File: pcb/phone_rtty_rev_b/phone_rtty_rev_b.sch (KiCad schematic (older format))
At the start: 33 parts, among them J1 Phone, J2 Transceiver, P1 TRX Data, Q1 2N2222, Q2 2N2222, SW1 1200/9600

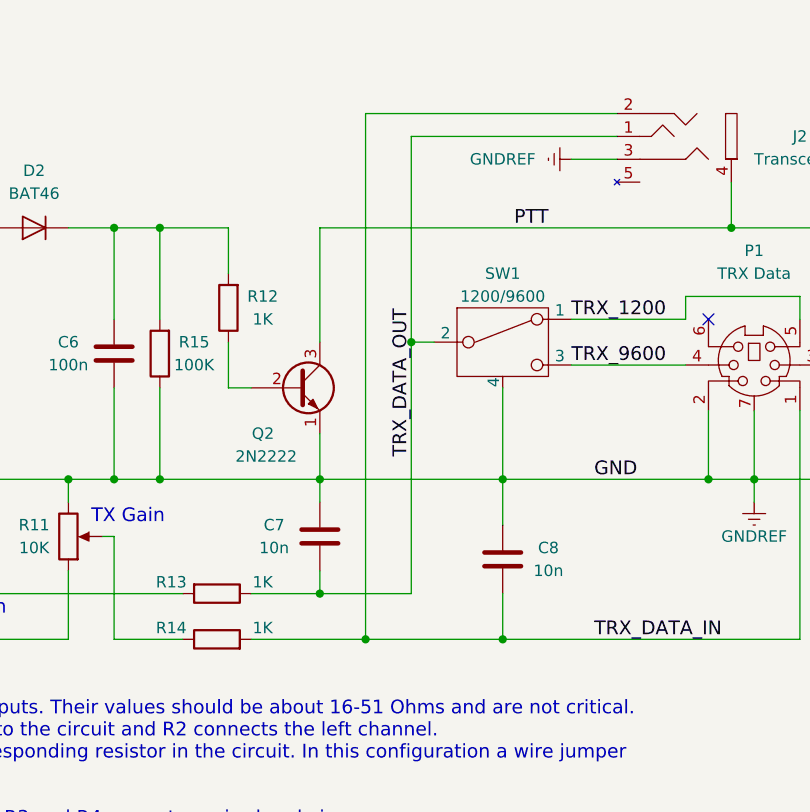
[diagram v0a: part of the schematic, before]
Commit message: Main board and panels corrections.
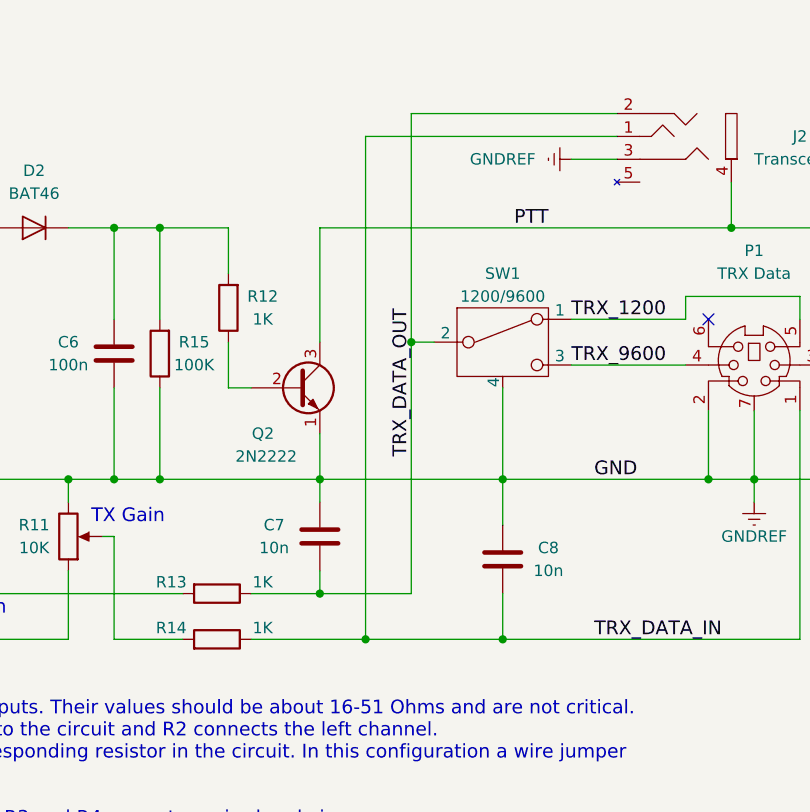
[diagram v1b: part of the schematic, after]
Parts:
- J1, J2: footprint custom_kicad_footprints:PJ320E_Headphones_Plug_Short -> Phone_RTTY_Footprints:PJ320E_3.5mm_Jack
- P1: footprint custom_kicad_footprints:Connector_Mini-DIN_Female_6Pin_2rows -> Phone_RTTY_Footprints:Connector_Mini-DIN_Female_6Pin_2rows
- R10, R11: footprint custom_kicad_footprints:Potentiometer_Trimmer_Vertical_Multi_Compatible -> Phone_RTTY_Footprints:Potentiometer_Trimmer_Vertical_Multi_Compatible
- SW1: footprint custom_kicad_footprints:Cliff_UT1x_SPDT_ON-ON_Switch_Short -> Phone_RTTY_Footprints:Cliff_UT1x_SPDT_ON-ON_Switch_Short
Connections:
- net GNDREF: now also C7.2, C8.2; no longer C7.1, C8.1
- net TRX_DATA_IN: now also C8.1, J2.1 (R), R14.1; no longer C8.2, J2.2 (L), R14.2
- net TRX_DATA_OUT: now also C7.1, J2.2 (L); no longer C7.2, J2.1 (R)
- net at R11.2: now also R14.2; no longer R14.1
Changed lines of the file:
@@
 U 1 1 5829EA63
 P 7900 3750
-F 0 "C8" H 8100 3800 50  0000 C CNN
-F 1 "10n" H 8100 3700 50  0000 C CNN
+F 0 "C8" H 8100 3700 50  0000 C CNN
+F 1 "10n" H 8100 3800 50  0000 C CNN
 F 2 "Capacitors_THT:C_Disc_D4.3mm_W1.9mm_P5.00mm" H 7938 3600 50  0001 C CNN
 F 3 "" H 7900 3750 50  0000 C CNN
 	1    7900 3750
-	1    0    0    -1
+	1    0    0    1
 $EndComp
 $Comp
@@
 U 1 1 5829EAA2
 P 7100 3650
-F 0 "C7" H 6900 3700 50  0000 C CNN
-F 1 "10n" H 6900 3600 50  0000 C CNN
+F 0 "C7" H 6900 3600 50  0000 C CNN
+F 1 "10n" H 6900 3700 50  0000 C CNN
 F 2 "Capacitors_THT:C_Disc_D4.3mm_W1.9mm_P5.00mm" H 7138 3500 50  0001 C CNN
 F 3 "" H 7100 3650 50  0000 C CNN
 	1    7100 3650
-	1    0    0    -1
+	1    0    0    1
 $EndComp
 $Comp
@@
 U 1 1 582ACA1A
 P 6650 4100
-F 0 "R14" V 6700 4300 50  0000 C CNN
-F 1 "1K" V 6700 3900 50  0000 C CNN
+F 0 "R14" V 6700 3900 50  0000 C CNN
+F 1 "1K" V 6700 4300 50  0000 C CNN
 F 2 "Resistors_THT:R_Axial_DIN0207_L6.3mm_D2.5mm_P10.16mm_Horizontal" V 6580 4100 50  0001 C CNN
 F 3 "" H 6650 4100 50  0000 C CNN
 	1    6650 4100
-	0    -1   -1   0
+	0    1    -1   0
 $EndComp
 $Comp
@@
 	7500 3900 6800 3900
 Wire Wire Line
-	7500 1900 7500 3900
+	7500 1800 7500 3900
 Wire Wire Line
 	7100 3800 7100 3900
@@
 F 0 "P1" H 9000 3400 50  0000 C CNN
 F 1 "TRX Data" H 9000 3300 50  0000 C CNN
-F 2 "custom_kicad_footprints:Connector_Mini-DIN_Female_6Pin_2rows" H 9000 2920 50  0001 C CNN
+F 2 "Phone_RTTY_Footprints:Connector_Mini-DIN_Female_6Pin_2rows" H 9000 2920 50  0001 C CNN
 F 3 "" H 9000 2920 50  0000 C CNN
 	1    9000 2900
@@
 F 0 "R11" H 5850 3600 50  0000 C CNN
 F 1 "10K" H 5850 3700 50  0000 C CNN
-F 2 "custom_kicad_footprints:Potentiometer_Trimmer_Vertical_Multi_Compatible" H 6000 3650 50  0001 C CNN
+F 2 "Phone_RTTY_Footprints:Potentiometer_Trimmer_Vertical_Multi_Compatible" H 6000 3650 50  0001 C CNN
 F 3 "" H 6000 3650 50  0000 C CNN
 	1    6000 3650
@@
 F 0 "R10" H 5350 3600 50  0000 C CNN
 F 1 "10K" H 5350 3700 50  0000 C CNN
-F 2 "custom_kicad_footprints:Potentiometer_Trimmer_Vertical_Multi_Compatible" H 5500 3650 50  0001 C CNN
+F 2 "Phone_RTTY_Footprints:Potentiometer_Trimmer_Vertical_Multi_Compatible" H 5500 3650 50  0001 C CNN
 F 3 "" H 5500 3650 50  0000 C CNN
 	1    5500 3650
@@
 F 0 "J1" H 2800 2900 50  0000 C CNN
 F 1 "Phone" H 2800 2800 50  0000 C CNN
-F 2 "custom_kicad_footprints:PJ320E_Headphones_Plug_Short" H 2600 2650 50  0001 C CNN
+F 2 "Phone_RTTY_Footprints:PJ320E_3.5mm_Jack" H 2600 2650 50  0001 C CNN
 F 3 "" H 2600 2650 50  0000 C CNN
 	1    2800 2500
@@
 F 0 "J2" H 9200 2100 50  0000 C CNN
 F 1 "Transceiver" H 9200 2000 50  0000 C CNN
-F 2 "custom_kicad_footprints:PJ320E_Headphones_Plug_Short" H 8400 2150 50  0001 C CNN
+F 2 "Phone_RTTY_Footprints:PJ320E_3.5mm_Jack" H 8400 2150 50  0001 C CNN
 F 3 "" H 8400 2150 50  0000 C CNN
 	1    8600 2000
@@
 F 0 "SW1" H 7900 3100 50  0000 C CNN
 F 1 "1200/9600" H 7900 3000 50  0000 C CNN
-F 2 "custom_kicad_footprints:Cliff_UT1x_SPDT_ON-ON_Switch_Short" H 7900 2800 50  0001 C CNN
+F 2 "Phone_RTTY_Footprints:Cliff_UT1x_SPDT_ON-ON_Switch_Short" H 7900 2800 50  0001 C CNN
 F 3 "" H 7900 2800 50  0000 C CNN
 	1    7900 2800
@@
 Text Label 7500 3300 1    60   ~ 0
 TRX_DATA_OUT
-Wire Wire Line
-	7300 4100 7300 1800
 Connection ~ 7300 4100
 Wire Wire Line
@@
 Connection ~ 8900 2300
 Wire Wire Line
-	8400 1900 7500 1900
-Wire Wire Line
-	7300 1800 8400 1800
-Wire Wire Line
 	3600 2400 3800 2400
 Connection ~ 3800 2400
@@
 	6200 3000 6200 3400
 Connection ~ 6200 3400
+Wire Wire Line
+	8400 1800 7500 1800
+Wire Wire Line
+	8400 1900 7300 1900
+Wire Wire Line
+	7300 1900 7300 4100
 $EndSCHEMATC
